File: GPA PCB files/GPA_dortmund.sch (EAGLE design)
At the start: 164 parts, among them U10 INA149SOIC8, U100 AAVID_TO220_HEATSINK, U101 AAVID_TO220_HEATSINK, U102 AAVID_TO220_HEATSINK, U103 AAVID_TO220_HEATSINK, U11 OPA549_KV_11TO-220_11, U12 OPA549_KV_11TO-220_11, U13 INA149SOIC8, U17 OPA549_KV_11TO-220_11, U18 OPA549_KV_11TO-220_11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

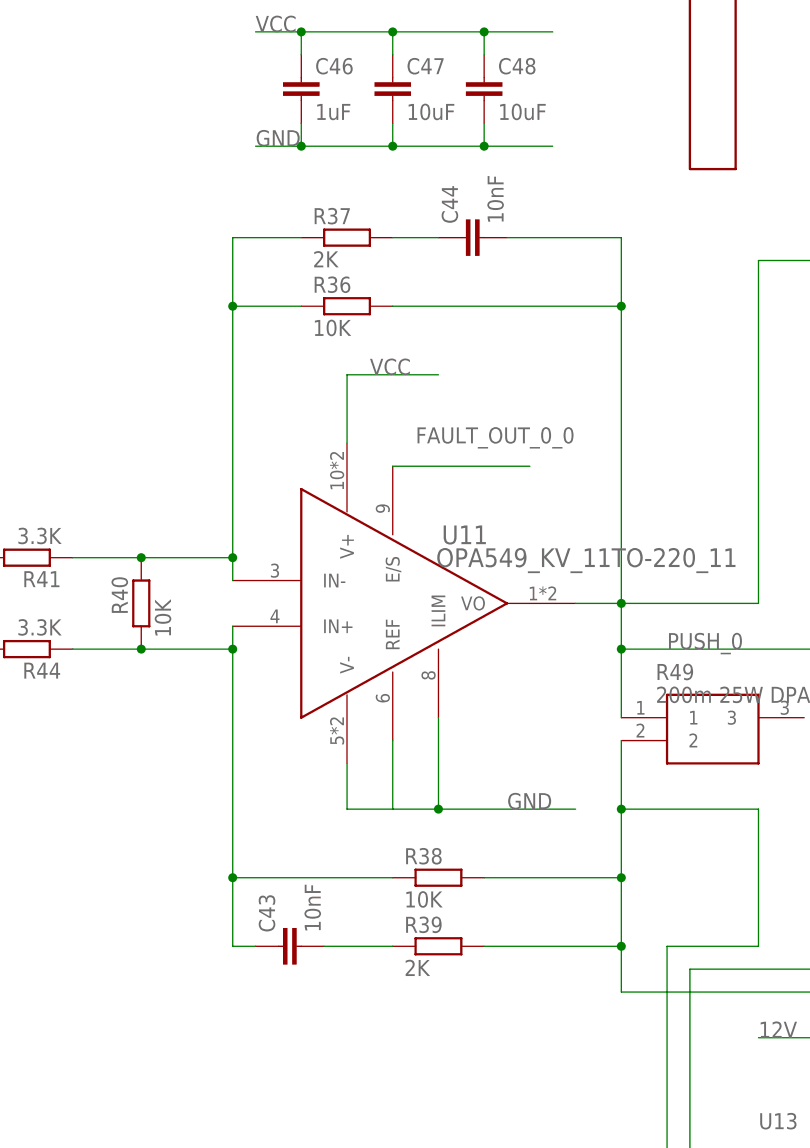
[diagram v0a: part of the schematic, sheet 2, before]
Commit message: -fixed values in schematic -fixed routines for saving and loading calibration data to eeprom
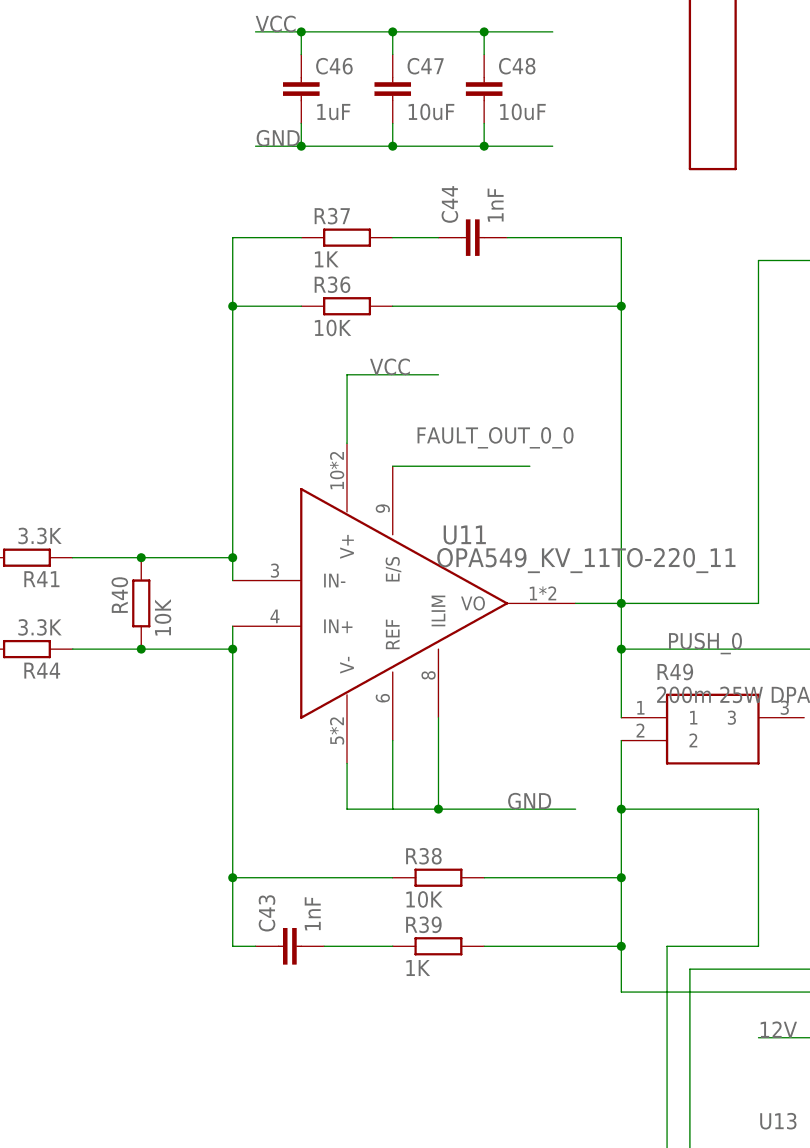
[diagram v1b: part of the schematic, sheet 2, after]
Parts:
- C43, C44: value 10nF -> 1nF
- R37, R39: value 2K -> 1K
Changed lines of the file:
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@@
 <part name="U12" library="my_parts" deviceset="OPA549_KV_11" device="TO-220_11"/>
 <part name="R36" library="rcl" library_urn="urn:adsk.eagle:library:334" deviceset="R-EU_" device="R0805" package3d_urn="urn:adsk.eagle:package:23553/2" value="10K"/>
-<part name="R37" library="rcl" library_urn="urn:adsk.eagle:library:334" deviceset="R-EU_" device="R0805" package3d_urn="urn:adsk.eagle:package:23553/2" value="2K"/>
+<part name="R37" library="rcl" library_urn="urn:adsk.eagle:library:334" deviceset="R-EU_" device="R0805" package3d_urn="urn:adsk.eagle:package:23553/2" value="1K"/>
 <part name="R38" library="rcl" library_urn="urn:adsk.eagle:library:334" deviceset="R-EU_" device="R0805" package3d_urn="urn:adsk.eagle:package:23553/2" value="10K"/>
-<part name="R39" library="rcl" library_urn="urn:adsk.eagle:library:334" deviceset="R-EU_" device="R0805" package3d_urn="urn:adsk.eagle:package:23553/2" value="2K"/>
-<part name="C43" library="rcl" library_urn="urn:adsk.eagle:library:334" deviceset="C-EU" device="C0805" package3d_urn="urn:adsk.eagle:package:23617/2" value="10nF"/>
-<part name="C44" library="rcl" library_urn="urn:adsk.eagle:library:334" deviceset="C-EU" device="C0805" package3d_urn="urn:adsk.eagle:package:23617/2" value="10nF"/>
+<part name="R39" library="rcl" library_urn="urn:adsk.eagle:library:334" deviceset="R-EU_" device="R0805" package3d_urn="urn:adsk.eagle:package:23553/2" value="1K"/>
+<part name="C43" library="rcl" library_urn="urn:adsk.eagle:library:334" deviceset="C-EU" device="C0805" package3d_urn="urn:adsk.eagle:package:23617/2" value="1nF"/>
+<part name="C44" library="rcl" library_urn="urn:adsk.eagle:library:334" deviceset="C-EU" device="C0805" package3d_urn="urn:adsk.eagle:package:23617/2" value="1nF"/>
 <part name="R40" library="rcl" library_urn="urn:adsk.eagle:library:334" deviceset="R-EU_" device="R0805" package3d_urn="urn:adsk.eagle:package:23553/2" value="10K"/>
 <part name="R41" library="rcl" library_urn="urn:adsk.eagle:library:334" deviceset="R-EU_" device="M0805" package3d_urn="urn:adsk.eagle:package:23556/2" value="3.3K"/>

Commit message: updated component values
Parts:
- C19, C28, C31, C32: value 1nF -> 100nF
- C45: value 10nF -> 1nF
- R41, R44: value 3.3K -> 10K
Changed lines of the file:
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@@
 <?xml version="1.0" encoding="utf-8"?>
 <!DOCTYPE eagle SYSTEM "eagle.dtd">
-<eagle version="9.4.2">
+<eagle version="9.5.2">
 <drawing>
 <settings>
@@
 <part name="C27" library="rcl" library_urn="urn:adsk.eagle:library:334" deviceset="C-EU" device="C0805" package3d_urn="urn:adsk.eagle:package:23617/2"/>
 <part name="R17" library="rcl" library_urn="urn:adsk.eagle:library:334" deviceset="R-EU_" device="M0805" package3d_urn="urn:adsk.eagle:package:23556/2" value="20"/>
-<part name="C28" library="rcl" library_urn="urn:adsk.eagle:library:334" deviceset="C-EU" device="C0805" package3d_urn="urn:adsk.eagle:package:23617/2" value="1nF"/>
+<part name="C28" library="rcl" library_urn="urn:adsk.eagle:library:334" deviceset="C-EU" device="C0805" package3d_urn="urn:adsk.eagle:package:23617/2" value="100nF"/>
 <part name="SV2" library="con-lstb" library_urn="urn:adsk.eagle:library:162" deviceset="MA03-1" device="" package3d_urn="urn:adsk.eagle:package:8339/1"/>
 <part name="U7" library="my_parts" deviceset="78L12" device=""/>
@@
 <part name="C7" library="rcl" library_urn="urn:adsk.eagle:library:334" deviceset="CPOL-EU" device="153CLV-1010" package3d_urn="urn:adsk.eagle:package:23413/2"/>
 <part name="SV3" library="con-lstb" library_urn="urn:adsk.eagle:library:162" deviceset="MA04-2" device="" package3d_urn="urn:adsk.eagle:package:8368/1"/>
-<part name="C19" library="rcl" library_urn="urn:adsk.eagle:library:334" deviceset="C-EU" device="C0805" package3d_urn="urn:adsk.eagle:package:23617/2" value="1nF"/>
-<part name="C31" library="rcl" library_urn="urn:adsk.eagle:library:334" deviceset="C-EU" device="C0805" package3d_urn="urn:adsk.eagle:package:23617/2" value="1nF"/>
-<part name="C32" library="rcl" library_urn="urn:adsk.eagle:library:334" deviceset="C-EU" device="C0805" package3d_urn="urn:adsk.eagle:package:23617/2" value="1nF"/>
+<part name="C19" library="rcl" library_urn="urn:adsk.eagle:library:334" deviceset="C-EU" device="C0805" package3d_urn="urn:adsk.eagle:package:23617/2" value="100nF"/>
+<part name="C31" library="rcl" library_urn="urn:adsk.eagle:library:334" deviceset="C-EU" device="C0805" package3d_urn="urn:adsk.eagle:package:23617/2" value="100nF"/>
+<part name="C32" library="rcl" library_urn="urn:adsk.eagle:library:334" deviceset="C-EU" device="C0805" package3d_urn="urn:adsk.eagle:package:23617/2" value="100nF"/>
 <part name="R1" library="rcl" library_urn="urn:adsk.eagle:library:334" deviceset="R-EU_" device="M0805" package3d_urn="urn:adsk.eagle:package:23556/2" value="20"/>
 <part name="R20" library="rcl" library_urn="urn:adsk.eagle:library:334" deviceset="R-EU_" device="M0805" package3d_urn="urn:adsk.eagle:package:23556/2" value="20"/>
@@
 <part name="C44" library="rcl" library_urn="urn:adsk.eagle:library:334" deviceset="C-EU" device="C0805" package3d_urn="urn:adsk.eagle:package:23617/2" value="1nF"/>
 <part name="R40" library="rcl" library_urn="urn:adsk.eagle:library:334" deviceset="R-EU_" device="R0805" package3d_urn="urn:adsk.eagle:package:23553/2" value="10K"/>
-<part name="R41" library="rcl" library_urn="urn:adsk.eagle:library:334" deviceset="R-EU_" device="M0805" package3d_urn="urn:adsk.eagle:package:23556/2" value="3.3K"/>
+<part name="R41" library="rcl" library_urn="urn:adsk.eagle:library:334" deviceset="R-EU_" device="M0805" package3d_urn="urn:adsk.eagle:package:23556/2" value="10K"/>
 <part name="R42" library="rcl" library_urn="urn:adsk.eagle:library:334" deviceset="R-EU_" device="R0805" package3d_urn="urn:adsk.eagle:package:23553/2" value="10K"/>
 <part name="R43" library="rcl" library_urn="urn:adsk.eagle:library:334" deviceset="R-EU_" device="R0805" package3d_urn="urn:adsk.eagle:package:23553/2" value="10K"/>
-<part name="R44" library="rcl" library_urn="urn:adsk.eagle:library:334" deviceset="R-EU_" device="R0805" package3d_urn="urn:adsk.eagle:package:23553/2" value="3.3K"/>
-<part name="C45" library="rcl" library_urn="urn:adsk.eagle:library:334" deviceset="C-EU" device="C0805" package3d_urn="urn:adsk.eagle:package:23617/2" value="10nF"/>
+<part name="R44" library="rcl" library_urn="urn:adsk.eagle:library:334" deviceset="R-EU_" device="R0805" package3d_urn="urn:adsk.eagle:package:23553/2" value="10K"/>
+<part name="C45" library="rcl" library_urn="urn:adsk.eagle:library:334" deviceset="C-EU" device="C0805" package3d_urn="urn:adsk.eagle:package:23617/2" value="1nF"/>
 <part name="R45" library="rcl" library_urn="urn:adsk.eagle:library:334" deviceset="R-EU_" device="R0805" package3d_urn="urn:adsk.eagle:package:23553/2" value="2K"/>
 <part name="R46" library="rcl" library_urn="urn:adsk.eagle:library:334" deviceset="R-EU_" device="R0805" package3d_urn="urn:adsk.eagle:package:23553/2" value="2K"/>

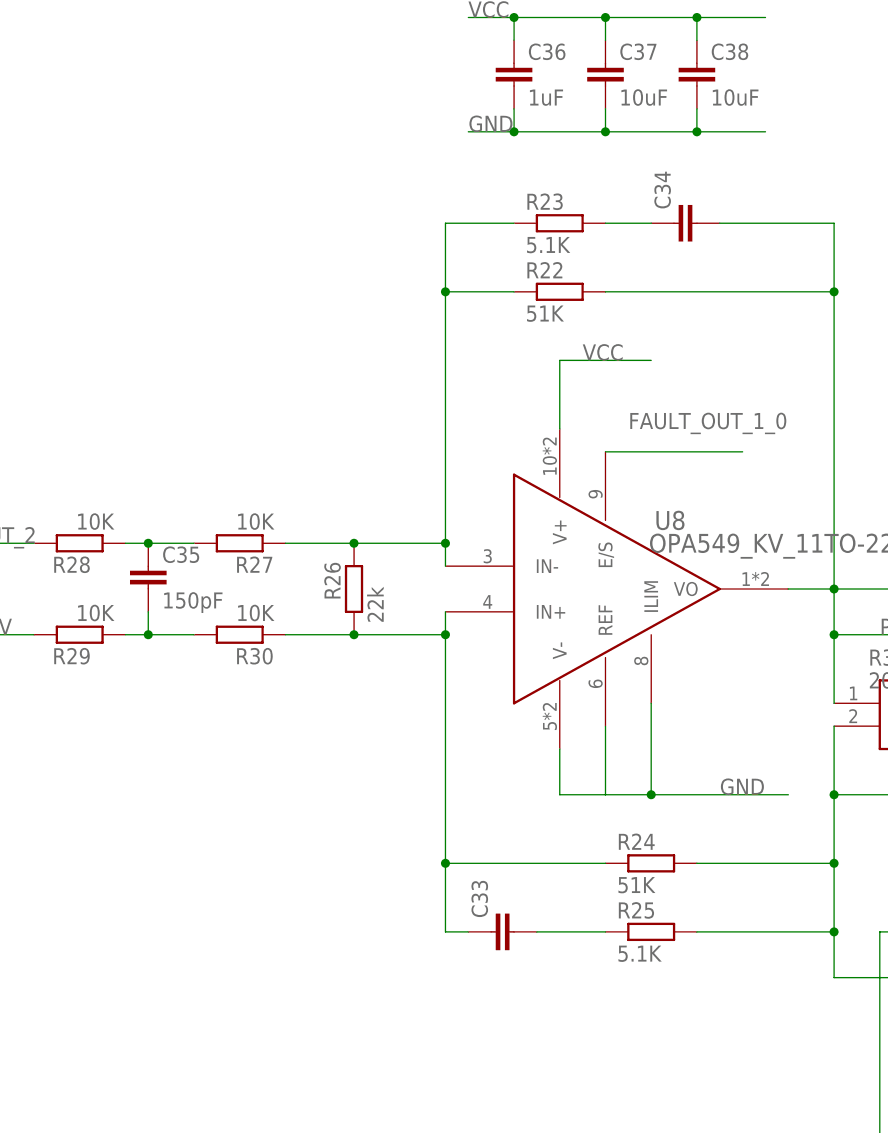
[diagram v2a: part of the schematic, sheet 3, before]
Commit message: updated component values
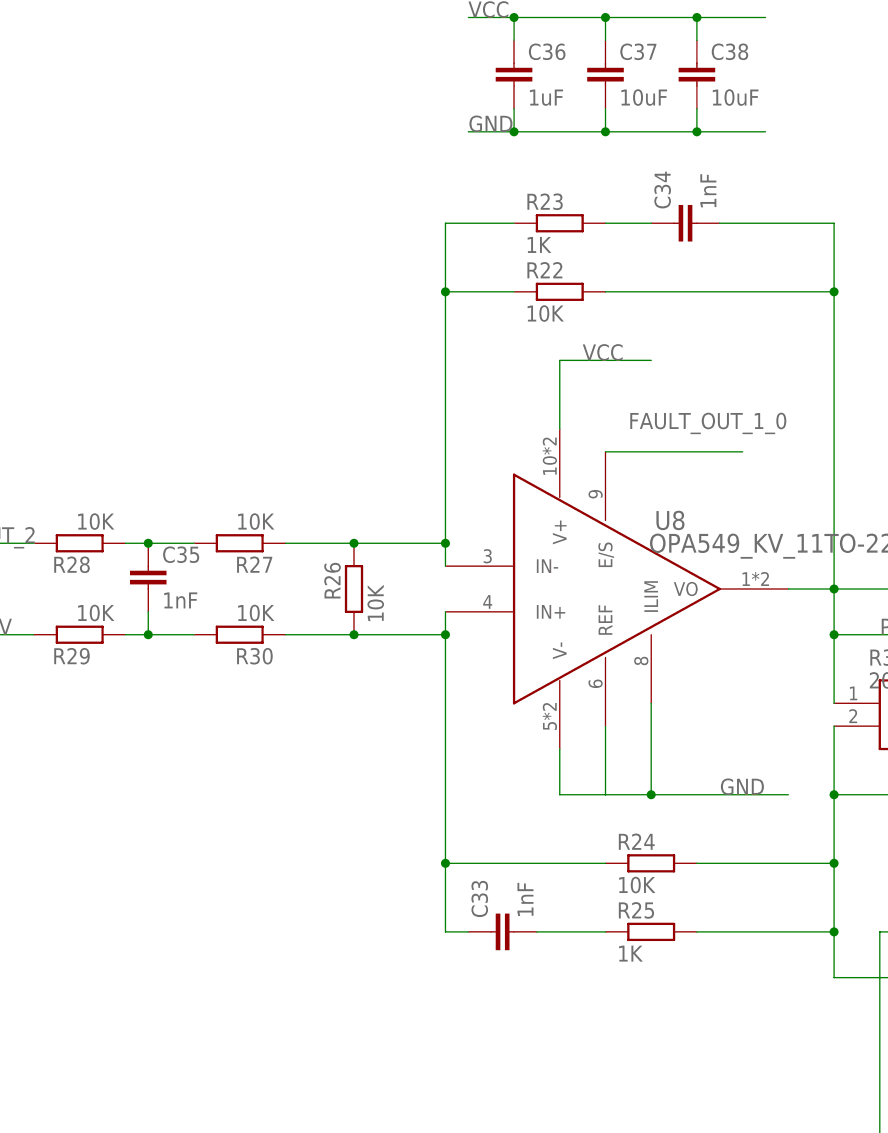
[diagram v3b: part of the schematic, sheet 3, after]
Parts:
- C33, C34, C63, C64, C83, C84: value (none) -> 1nF
- C35, C65, C85: value 150pF -> 1nF
- R22, R24, R64, R66, R92, R94: value 51K -> 10K
- R23, R25, R65, R67, R93, R95: value 5.1K -> 1K
- R26, R68, R96: value 22k -> 10K
